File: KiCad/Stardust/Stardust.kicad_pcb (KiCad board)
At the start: 2 copper layers, 77 x 77 mm, 44 parts, among them J1 12V DC, J2 RJ12, J3 1x2 Connector, J4 Conn_01x04_Pin, J5 Conn_01x04_Pin, J6 1x3 Header, J7 1x2 Connector, J8 Conn_01x19_Pin, U1 ESP32, U2 BTT TMC2209 V1.3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

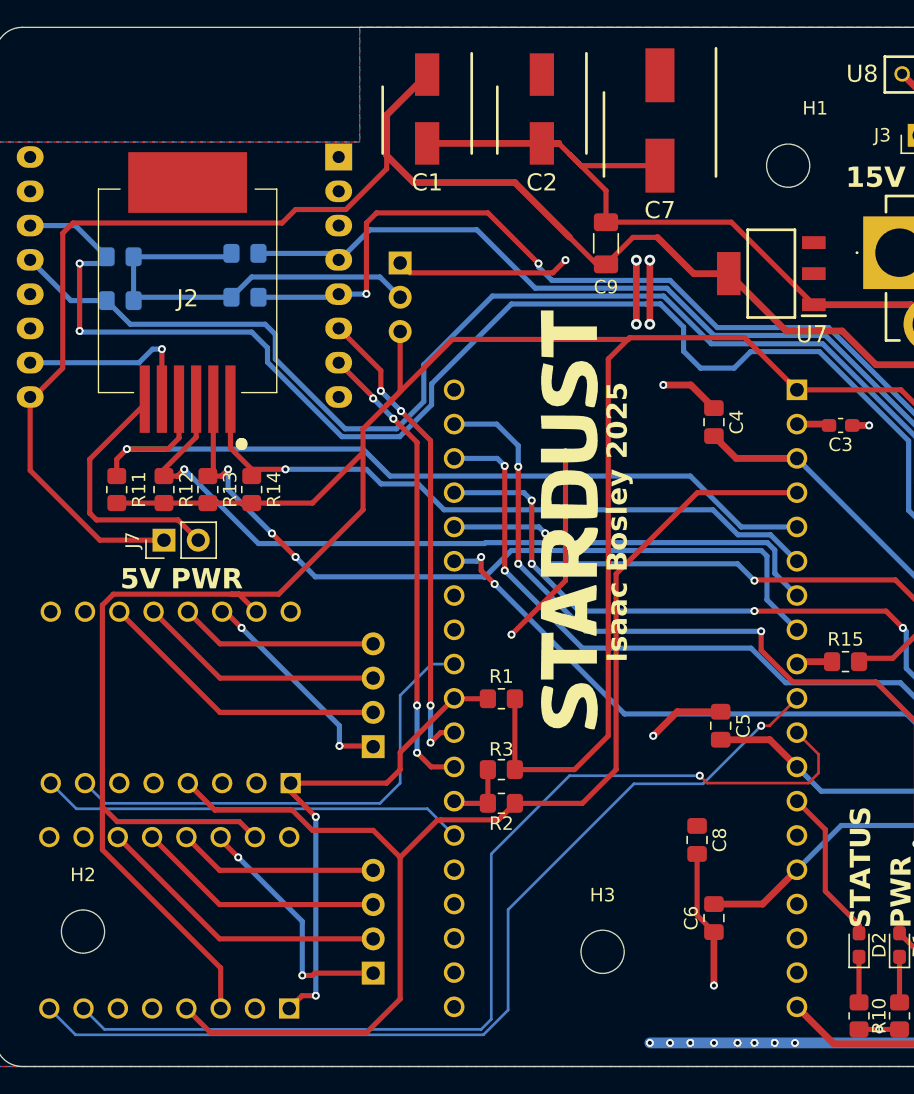
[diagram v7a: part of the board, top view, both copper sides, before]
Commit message: Started revising board. Did stepper drivers and updated some footprints
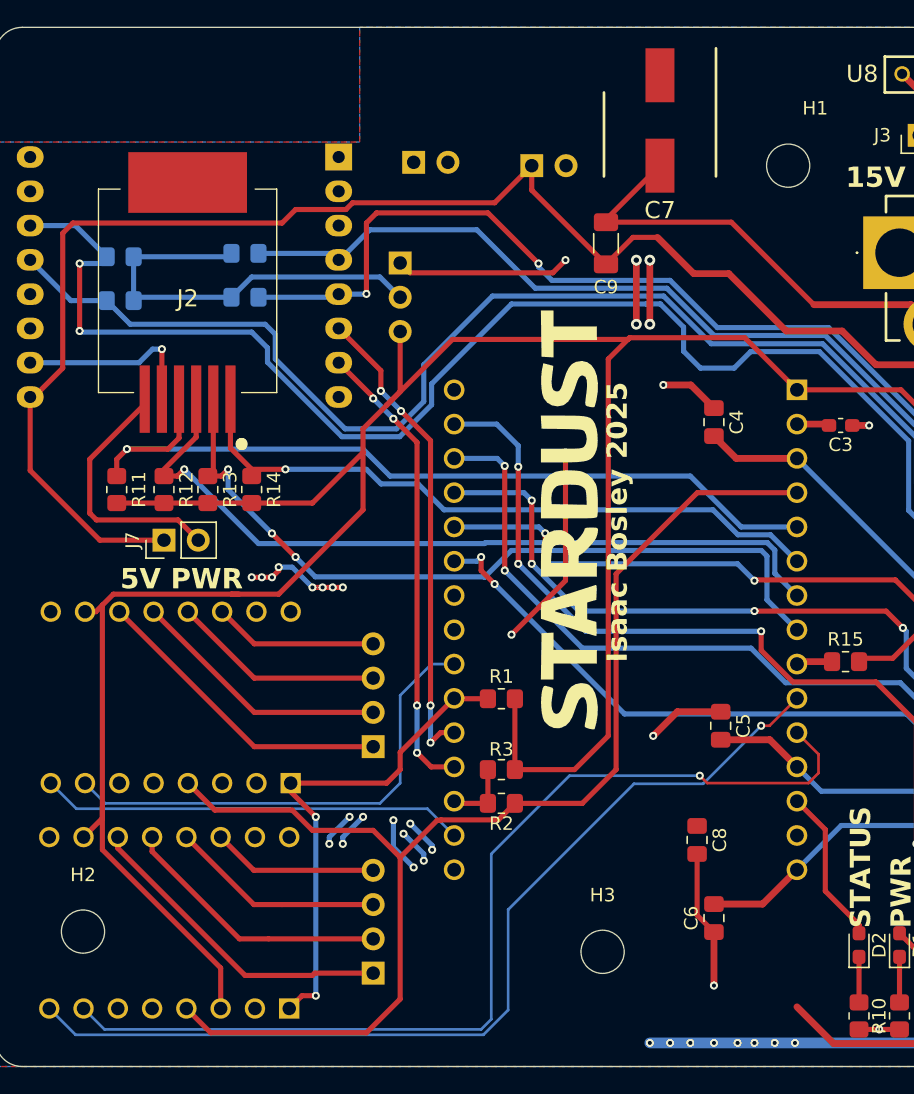
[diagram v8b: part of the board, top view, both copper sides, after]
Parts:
- removed C1, C2: 10 uF, Stardust:10uFElectrolyticCap_CAPAE660X550N
- removed U7: Regulator - 5V 1A, Stardust:5VREG_SOT230P700X180-4N
- added J10: 12V OUT, Connector_PinHeader_2.54mm:PinHeader_1x02_P2.54mm_Vertical, B.Cu at (154.0, 60.0)
- added J9: 5V IN, Connector_PinHeader_2.54mm:PinHeader_1x02_P2.54mm_Vertical, B.Cu at (162.8, 60.2)
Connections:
- J4 pad 2: /A2_1 -> /B1_1
- J4 pad 4: /B1_1 -> /A2_1
- J5 pad 2: /A2_2 -> /B1_2
- J5 pad 4: /B1_2 -> /A2_2
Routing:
- net +12V: track 33.1 -> 55.6 mm, vias 15 -> 33
- net GND: track 128.7 -> 109.2 mm
- net +3.3V: track 238.1 -> 228.3 mm
- net /A2_2: track 22.0 -> 12.5 mm
- net /A2_1: track 21.9 -> 12.4 mm
- net /B2_1: track 16.2 -> 23.0 mm, vias 2 -> 0
- net +5V: track 191.7 -> 185.0 mm
- net /B2_2: track 18.1 -> 23.7 mm, vias 2 -> 0
- net /B1_2: track 14.9 -> 20.1 mm
- net /B1_1: track 14.7 -> 19.4 mm
- net /A1_1: track 18.3 -> 15.8 mm
- net /A1_2: track 18.5 -> 15.9 mm
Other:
- board text added: "12V+"
- board text added: "5V+"
